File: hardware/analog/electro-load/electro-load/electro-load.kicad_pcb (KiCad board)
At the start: 2 copper layers, 178 x 119 mm, 144 parts, among them J1 AVR-ISP-10, J2 Conn_WallSocket_Earth, J3 INPUT, J4 INPUT, K1 SANYOU_SRD_Form_C, M1 Noctua NF-A14 5V, Q1 2N2222A, Q2 2N2222A, Q3 IPP037N06L3, Q4 IPP037N06L3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

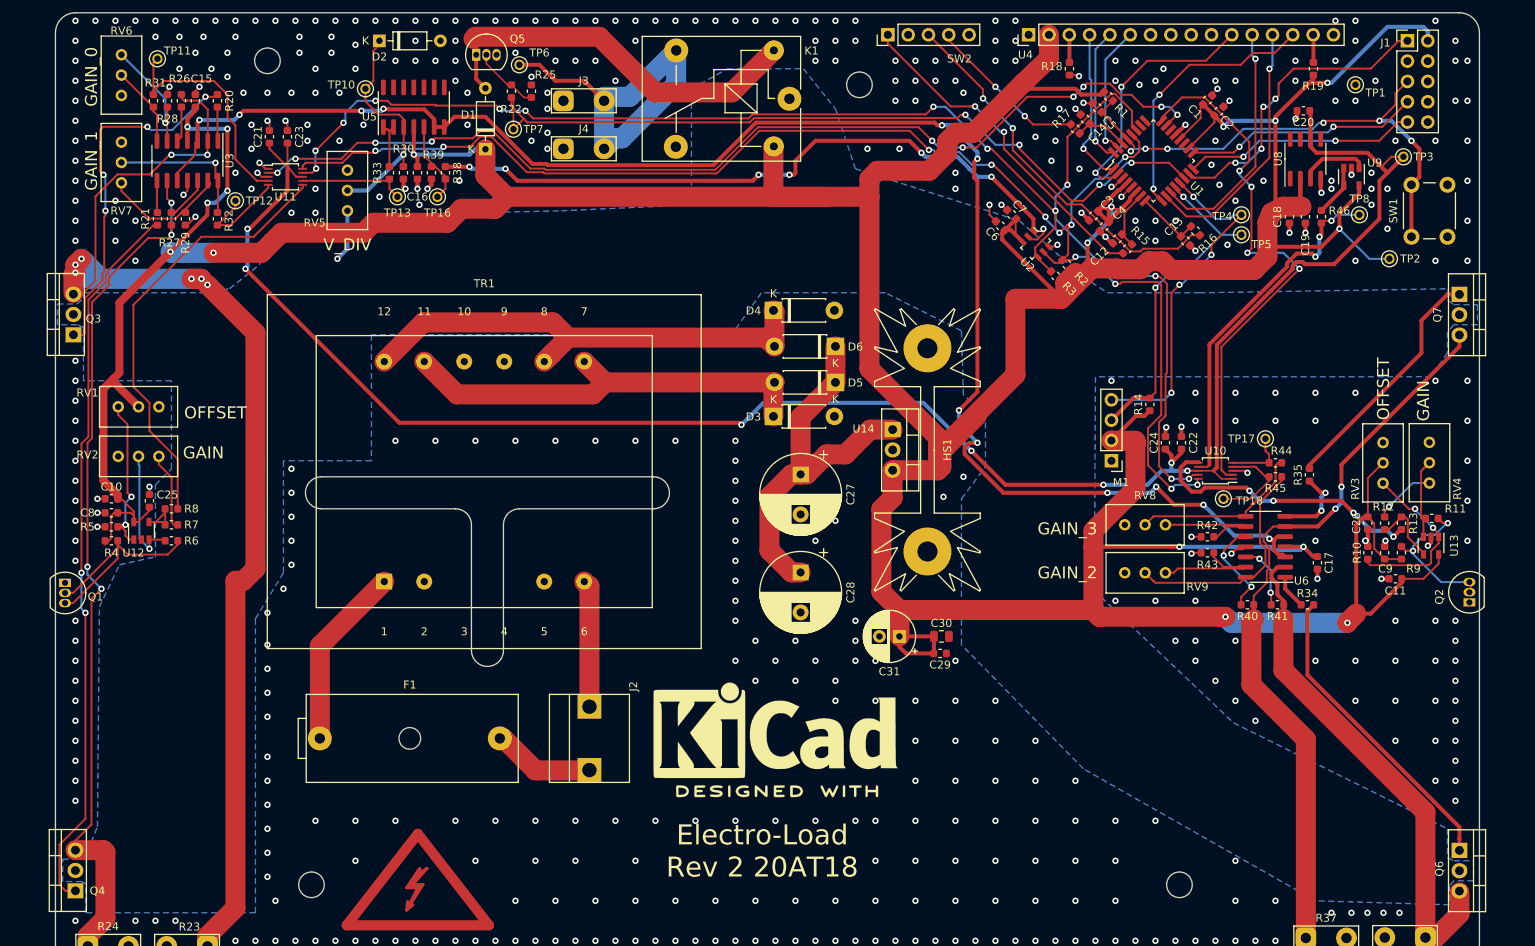
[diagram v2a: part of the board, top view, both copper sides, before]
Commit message: Added extra footprints for temperature probes - 2N4921
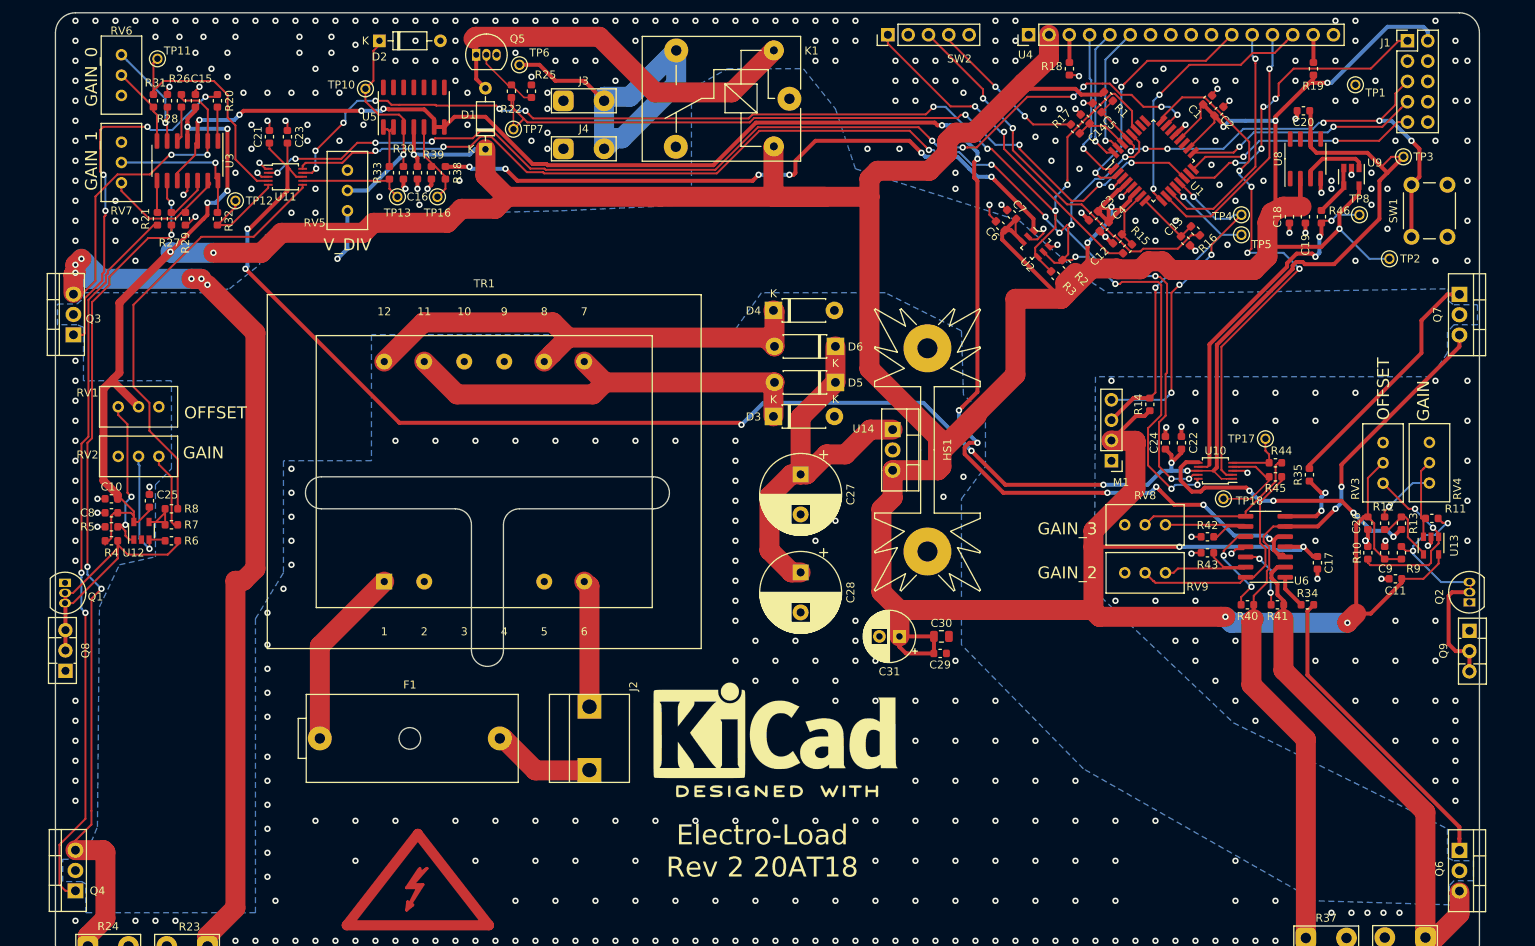
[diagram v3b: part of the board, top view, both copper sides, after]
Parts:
- removed the REF** at (89.0, 35.0)
- removed the REF** at (163.0, 38.0)
- removed the REF** at (203.0, 138.0)
- removed the REF** at (94.5, 138.0)
- added Q8: 2N4921, Package_TO_SOT_THT:TO-126-3_Vertical, F.Cu at (63.8, 111.2)
- added Q9: 2N4921, Package_TO_SOT_THT:TO-126-3_Vertical, F.Cu at (239.2, 106.2)
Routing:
- net Net-(Q2-Pad2): track 19.4 -> 34.2 mm
- net Net-(Q1-Pad2): track 29.9 -> 37.2 mm
- net GND: vias 481 -> 477
- net (no net): vias 17 -> 13

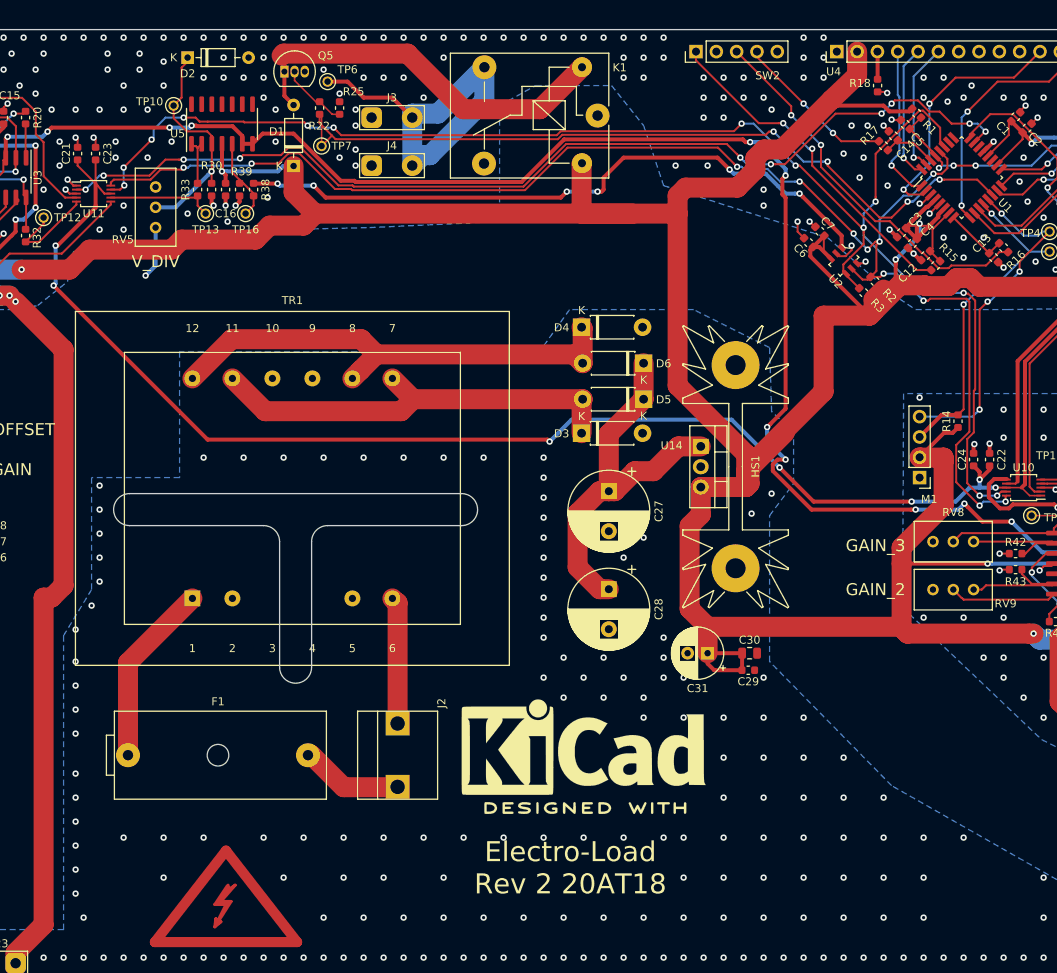
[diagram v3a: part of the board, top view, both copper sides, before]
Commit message: Added mounting holes to schematic as well. Also made them solid ground anchors.
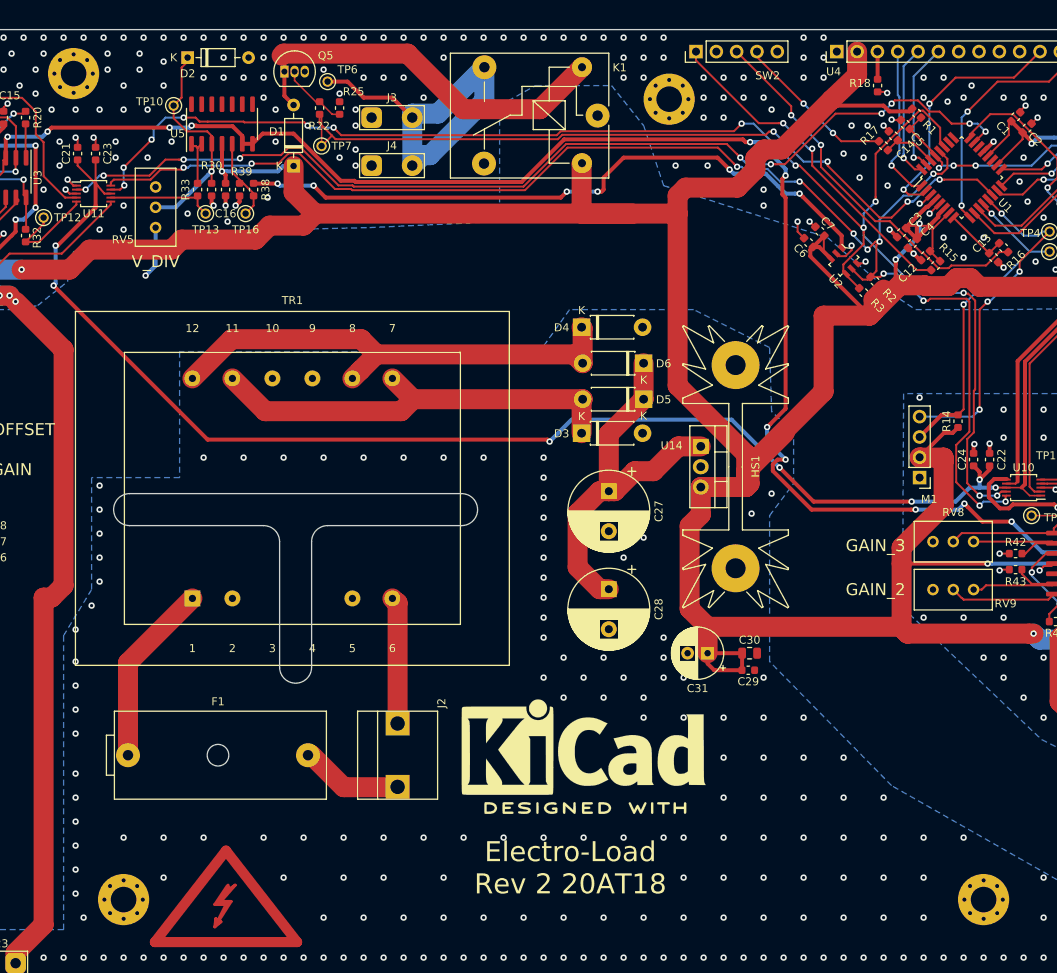
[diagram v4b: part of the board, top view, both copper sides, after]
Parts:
- added H1: MountingHole_Pad, MountingHole:MountingHole_3.2mm_M3_Pad_Via, F.Cu at (95.0, 137.8)
- added H2: MountingHole_Pad, MountingHole:MountingHole_3.2mm_M3_Pad_Via, F.Cu at (88.8, 34.5)
- added H3: MountingHole_Pad, MountingHole:MountingHole_3.2mm_M3_Pad_Via, F.Cu at (202.5, 137.8)
- added H4: MountingHole_Pad, MountingHole:MountingHole_3.2mm_M3_Pad_Via, F.Cu at (163.2, 37.7)
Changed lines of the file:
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@@
     (tracks 2039)
     (zones 0)
-    (modules 142)
+    (modules 146)
     (nets 89)
   )
@@
   )
   (setup
-    (last_trace_width 0.5)
+    (last_trace_width 0.25)
     (user_trace_width 0.2)
     (user_trace_width 0.5)
@@
     (mod_text_size 1 1)
     (mod_text_width 0.15)
-    (pad_size 1.905 2)
-    (pad_drill 1.1)
+    (pad_size 6.4 6.4)
+    (pad_drill 3.2)
     (pad_to_mask_clearance 0.051)
     (solder_mask_min_width 0.25)
@@
     (add_net "/Current Measurements/LOAD_CURRENT")
   )
+  (module MountingHole:MountingHole_3.2mm_M3_Pad_Via (layer F.Cu)
+    (at 163.197056 37.697056)
+    (descr "Mounting Hole 3.2mm, M3")
+    (tags "mounting hole 3.2mm m3")
+    (zone_connect 2)
+    (attr virtual)
+    (fp_text reference H4 (at 0 -4.2) (layer F.SilkS) hide
+      (effects (font (size 1 1) (thickness 0.15)))
+    )
+    (fp_text value MountingHole_Pad (at 0 4.2) (layer F.Fab)
+      (effects (font (size 1 1) (thickness 0.15)))
+    )
+    (fp_circle (center 0 0) (end 3.45 0) (layer F.CrtYd) (width 0.05))
+    (fp_circle (center 0 0) (end 3.2 0) (layer Cmts.User) (width 0.15))
+    (fp_text user %R (at 0.3 0) (layer F.Fab)
+      (effects (font (size 1 1) (thickness 0.15)))
+    )
+    (pad 1 thru_hole circle (at 1.697056 -1.697056) (size 0.8 0.8) (drill 0.5) (layers *.Cu *.Mask)
+      (net 1 GND) (zone_connect 2))
+    (pad 1 thru_hole circle (at 0 -2.4) (size 0.8 0.8) (drill 0.5) (layers *.Cu *.Mask)
+      (net 1 GND) (zone_connect 2))
+    (pad 1 thru_hole circle (at -1.697056 -1.697056) (size 0.8 0.8) (drill 0.5) (layers *.Cu *.Mask)
+      (net 1 GND) (zone_connect 2))
+    (pad 1 thru_hole circle (at -2.4 0) (size 0.8 0.8) (drill 0.5) (layers *.Cu *.Mask)
+      (net 1 GND) (zone_connect 2))
+    (pad 1 thru_hole circle (at -1.697056 1.697056) (size 0.8 0.8) (drill 0.5) (layers *.Cu *.Mask)
+      (net 1 GND) (zone_connect 2))
+    (pad 1 thru_hole circle (at 0 2.4) (size 0.8 0.8) (drill 0.5) (layers *.Cu *.Mask)
+      (net 1 GND) (zone_connect 2))
+    (pad 1 thru_hole circle (at 1.697056 1.697056) (size 0.8 0.8) (drill 0.5) (layers *.Cu *.Mask)
+      (net 1 GND) (zone_connect 2))
+    (pad 1 thru_hole circle (at 2.4 0) (size 0.8 0.8) (drill 0.5) (layers *.Cu *.Mask)
+      (net 1 GND) (zone_connect 2))
+    (pad 1 thru_hole circle (at 0 0) (size 6.4 6.4) (drill 3.2) (layers *.Cu *.Mask)
+      (net 1 GND) (zone_connect 2))
+  )
+  (module MountingHole:MountingHole_3.2mm_M3_Pad_Via (layer F.Cu)
+    (at 202.5 137.75)
+    (descr "Mounting Hole 3.2mm, M3")
+    (tags "mounting hole 3.2mm m3")
+    (attr virtual)
+    (fp_text reference H3 (at 0 -4.2) (layer F.SilkS) hide
+      (effects (font (size 1 1) (thickness 0.15)))
+    )
+    (fp_text value MountingHole_Pad (at 0 4.2) (layer F.Fab)
+      (effects (font (size 1 1) (thickness 0.15)))
+    )
+    (fp_circle (center 0 0) (end 3.45 0) (layer F.CrtYd) (width 0.05))
+    (fp_circle (center 0 0) (end 3.2 0) (layer Cmts.User) (width 0.15))
+    (fp_text user %R (at 0.3 0) (layer F.Fab)
+      (effects (font (size 1 1) (thickness 0.15)))
+    )
+    (pad 1 thru_hole circle (at 1.697056 -1.697056) (size 0.8 0.8) (drill 0.5) (layers *.Cu *.Mask)
+      (net 1 GND))
+    (pad 1 thru_hole circle (at 0 -2.4) (size 0.8 0.8) (drill 0.5) (layers *.Cu *.Mask)
+      (net 1 GND))
+    (pad 1 thru_hole circle (at -1.697056 -1.697056) (size 0.8 0.8) (drill 0.5) (layers *.Cu *.Mask)
+      (net 1 GND))
+    (pad 1 thru_hole circle (at -2.4 0) (size 0.8 0.8) (drill 0.5) (layers *.Cu *.Mask)
+      (net 1 GND))
+    (pad 1 thru_hole circle (at -1.697056 1.697056) (size 0.8 0.8) (drill 0.5) (layers *.Cu *.Mask)
+      (net 1 GND))
+    (pad 1 thru_hole circle (at 0 2.4) (size 0.8 0.8) (drill 0.5) (layers *.Cu *.Mask)
+      (net 1 GND))
+    (pad 1 thru_hole circle (at 1.697056 1.697056) (size 0.8 0.8) (drill 0.5) (layers *.Cu *.Mask)
+      (net 1 GND))
+    (pad 1 thru_hole circle (at 2.4 0) (size 0.8 0.8) (drill 0.5) (layers *.Cu *.Mask)
+      (net 1 GND))
+    (pad 1 thru_hole circle (at 0 0) (size 6.4 6.4) (drill 3.2) (layers *.Cu *.Mask)
+      (net 1 GND) (zone_connect 2))
+  )
+  (module MountingHole:MountingHole_3.2mm_M3_Pad_Via (layer F.Cu)
+    (at 88.75 34.5)
+    (descr "Mounting Hole 3.2mm, M3")
+    (tags "mounting hole 3.2mm m3")
+    (attr virtual)
+    (fp_text reference H2 (at 0 -4.2) (layer F.SilkS) hide
+      (effects (font (size 1 1) (thickness 0.15)))
+    )
+    (fp_text value MountingHole_Pad (at 0 4.2) (layer F.Fab)
+      (effects (font (size 1 1) (thickness 0.15)))
+    )
+    (fp_circle (center 0 0) (end 3.45 0) (layer F.CrtYd) (width 0.05))
+    (fp_circle (center 0 0) (end 3.2 0) (layer Cmts.User) (width 0.15))
+    (fp_text user %R (at 0.3 0) (layer F.Fab)
+      (effects (font (size 1 1) (thickness 0.15)))
+    )
+    (pad 1 thru_hole circle (at 1.697056 -1.697056) (size 0.8 0.8) (drill 0.5) (layers *.Cu *.Mask)
+      (net 1 GND))
+    (pad 1 thru_hole circle (at 0 -2.4) (size 0.8 0.8) (drill 0.5) (layers *.Cu *.Mask)
+      (net 1 GND))
+    (pad 1 thru_hole circle (at -1.697056 -1.697056) (size 0.8 0.8) (drill 0.5) (layers *.Cu *.Mask)
+      (net 1 GND))
+    (pad 1 thru_hole circle (at -2.4 0) (size 0.8 0.8) (drill 0.5) (layers *.Cu *.Mask)
+      (net 1 GND))
+    (pad 1 thru_hole circle (at -1.697056 1.697056) (size 0.8 0.8) (drill 0.5) (layers *.Cu *.Mask)
+      (net 1 GND))
+    (pad 1 thru_hole circle (at 0 2.4) (size 0.8 0.8) (drill 0.5) (layers *.Cu *.Mask)
+      (net 1 GND))
+    (pad 1 thru_hole circle (at 1.697056 1.697056) (size 0.8 0.8) (drill 0.5) (layers *.Cu *.Mask)
+      (net 1 GND))
+    (pad 1 thru_hole circle (at 2.4 0) (size 0.8 0.8) (drill 0.5) (layers *.Cu *.Mask)
+      (net 1 GND))
+    (pad 1 thru_hole circle (at 0 0) (size 6.4 6.4) (drill 3.2) (layers *.Cu *.Mask)
+      (net 1 GND) (zone_connect 2))
+  )
+  (module MountingHole:MountingHole_3.2mm_M3_Pad_Via (layer F.Cu)
+    (at 95 137.75)
+    (descr "Mounting Hole 3.2mm, M3")
+    (tags "mounting hole 3.2mm m3")
+    (zone_connect 2)
+    (attr virtual)
+    (fp_text reference H1 (at 0 -4.2) (layer F.SilkS) hide
+      (effects (font (size 1 1) (thickness 0.15)))
+    )
+    (fp_text value MountingHole_Pad (at 0 4.2) (layer F.Fab)
+      (effects (font (size 1 1) (thickness 0.15)))
+    )
+    (fp_circle (center 0 0) (end 3.45 0) (layer F.CrtYd) (width 0.05))
+    (fp_circle (center 0 0) (end 3.2 0) (layer Cmts.User) (width 0.15))
+    (fp_text user %R (at 0.3 0) (layer F.Fab)
+      (effects (font (size 1 1) (thickness 0.15)))
+    )
+    (pad 1 thru_hole circle (at 1.697056 -1.697056) (size 0.8 0.8) (drill 0.5) (layers *.Cu *.Mask)
+      (net 1 GND) (zone_connect 2))
+    (pad 1 thru_hole circle (at 0 -2.4) (size 0.8 0.8) (drill 0.5) (layers *.Cu *.Mask)
+      (net 1 GND) (zone_connect 2))
+    (pad 1 thru_hole circle (at -1.697056 -1.697056) (size 0.8 0.8) (drill 0.5) (layers *.Cu *.Mask)
+      (net 1 GND) (zone_connect 2))
+    (pad 1 thru_hole circle (at -2.4 0) (size 0.8 0.8) (drill 0.5) (layers *.Cu *.Mask)
+      (net 1 GND) (zone_connect 2))
+    (pad 1 thru_hole circle (at -1.697056 1.697056) (size 0.8 0.8) (drill 0.5) (layers *.Cu *.Mask)
+      (net 1 GND) (zone_connect 2))
+    (pad 1 thru_hole circle (at 0 2.4) (size 0.8 0.8) (drill 0.5) (layers *.Cu *.Mask)
+      (net 1 GND) (zone_connect 2))
+    (pad 1 thru_hole circle (at 1.697056 1.697056) (size 0.8 0.8) (drill 0.5) (layers *.Cu *.Mask)
+      (net 1 GND) (zone_connect 2))
+    (pad 1 thru_hole circle (at 2.4 0) (size 0.8 0.8) (drill 0.5) (layers *.Cu *.Mask)
+      (net 1 GND) (zone_connect 2))
+    (pad 1 thru_hole circle (at 0 0) (size 6.4 6.4) (drill 3.2) (layers *.Cu *.Mask)
+      (net 1 GND) (zone_connect 2))
+  )
   (module Package_TO_SOT_THT:TO-126-3_Vertical (layer F.Cu)
